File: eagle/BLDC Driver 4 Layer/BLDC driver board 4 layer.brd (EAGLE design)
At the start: 38 parts, among them Q1 CSD173XXQX-NEXFET, Q11 CSD173XXQX-NEXFET, Q3 CSD173XXQX-NEXFET, Q5 CSD173XXQX-NEXFET, Q7 CSD173XXQX-NEXFET, Q9 CSD173XXQX-NEXFET

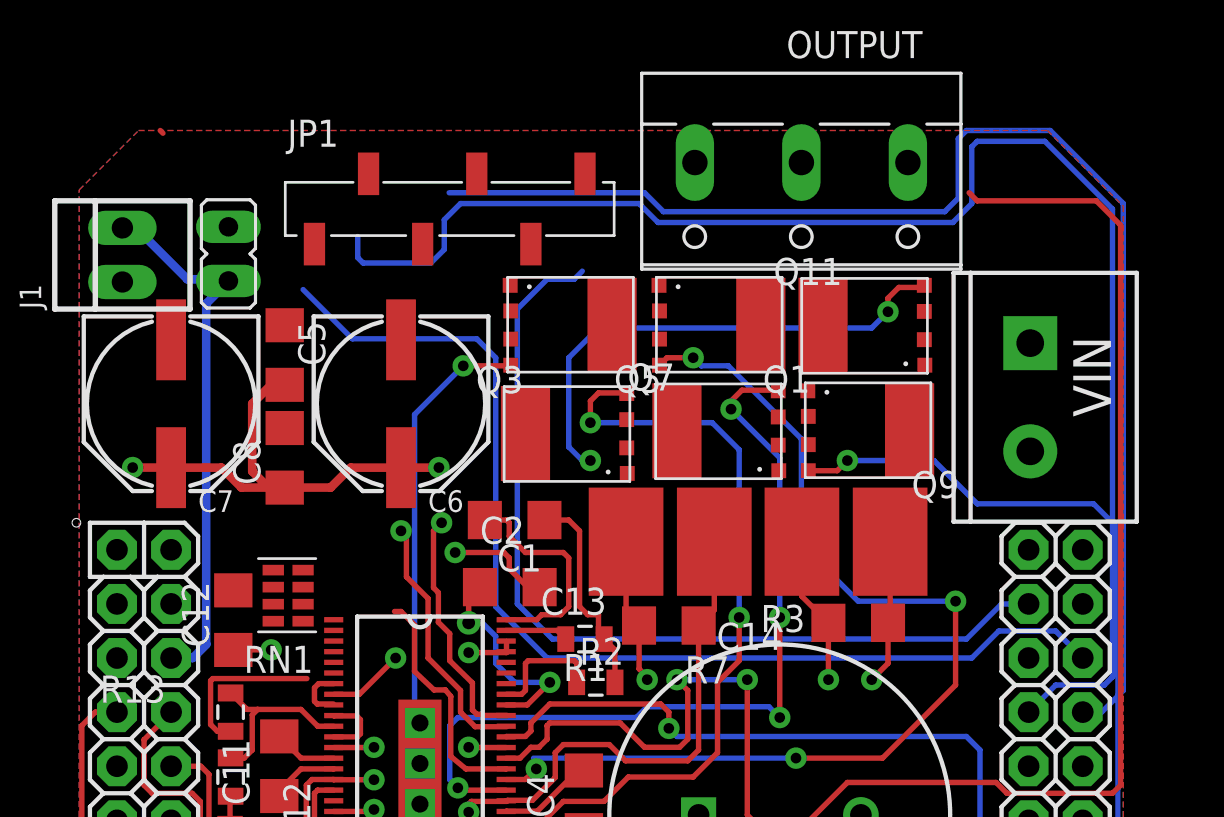
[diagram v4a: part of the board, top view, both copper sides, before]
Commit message: Changes to bldc 4-layer. Finished ethershield v3.
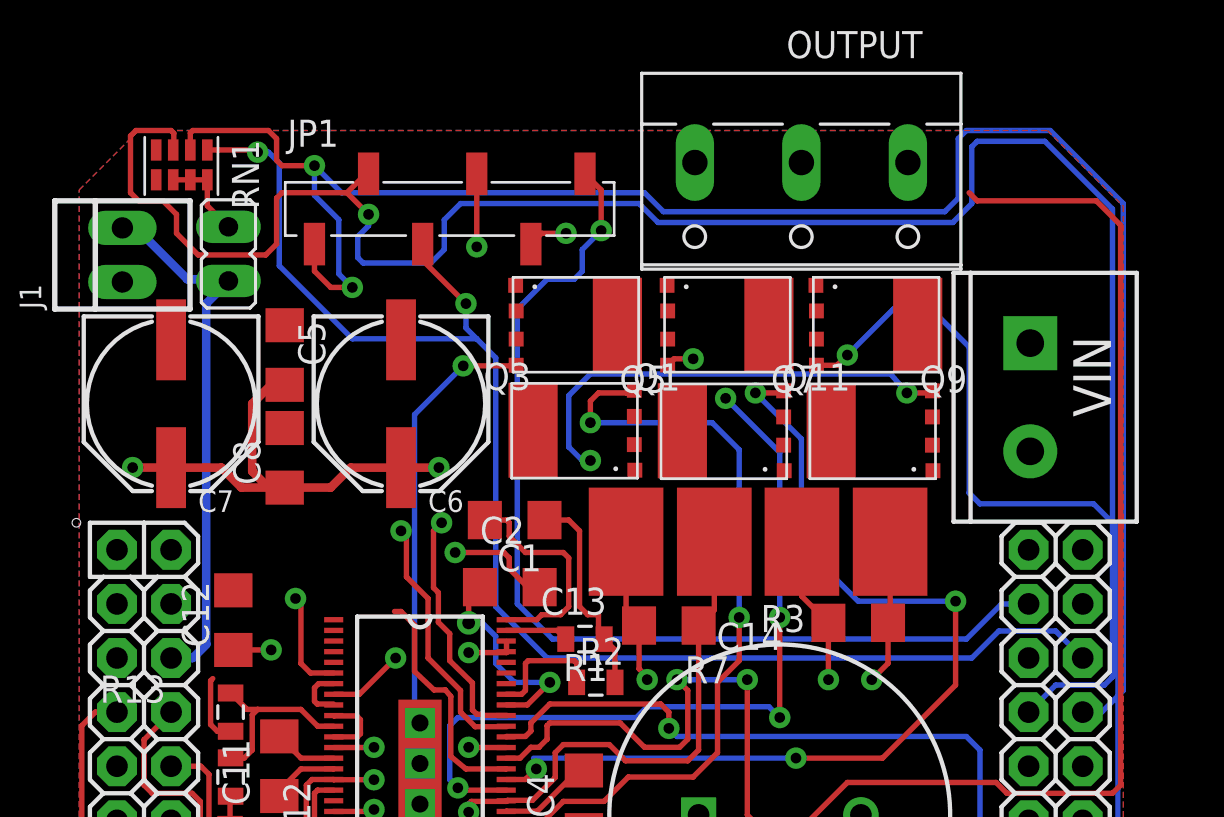
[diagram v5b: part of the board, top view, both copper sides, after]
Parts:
- moved RN1 22.6 mm to (8.69, 42.9), turned to 180 degrees
- moved Q7 6.57 mm to (35.1, 34.7), turned to 180 degrees
- moved Q1 6.17 mm to (31.0, 29.7), turned to 0 degrees
- moved Q11 4.97 mm to (38.0, 29.7)
- moved Q9 4.97 mm to (42.0, 34.7)
- moved Q3 0.39 mm to (24.0, 29.7)
- moved Q5 0.25 mm to (27.9, 34.7)
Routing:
- net ADC/HALL1: track 61.8 -> 86.5 mm, vias 0 -> 2
- net ADC/HALL2: track 70.1 -> 94.0 mm, vias 0 -> 1
- net QEI-A: track 26.4 -> 49.2 mm, vias 0 -> 1
- net N$2: track 0.00 -> 19.3 mm, vias 0 -> 1
- net ADC/HALL3: track 51.7 -> 67.2 mm, vias 0 -> 2
- net GL_A: track 71.7 -> 79.2 mm
- net QEI-INDEX: track 43.0 -> 48.3 mm, vias 0 -> 1
- net QEI-B: track 47.6 -> 52.7 mm, vias 0 -> 1
- net GND: track 24.3 -> 19.9 mm
- net N$13: track 0.00 -> 4.22 mm
- net GH_B: track 58.1 -> 54.1 mm
- net GH_A: track 43.7 -> 41.3 mm
- net GL_B: track 39.7 -> 41.8 mm, vias 4 -> 5

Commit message: Removed dependencies from ASL.lbr in /Boards.
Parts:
- DRV8301: device ASL:HTSSOP56 -> pavlo:HTSSOP56
- Q1, Q11, Q3, Q5, Q7, Q9: device ASL:CSD173XXQX -> pavlo:CSD173XXQX
- R3, R7: device ASL:SMT-REF -> pavlo:SMT-REF
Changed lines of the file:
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@@
 <?xml version="1.0" encoding="utf-8"?>
 <!DOCTYPE eagle SYSTEM "eagle.dtd">
-<eagle version="6.3">
+<eagle version="6.1">
 <drawing>
 <settings>
@@
 </class>
 </classes>
-<designrules name="default">
+<designrules>
 <description language="en">&lt;b&gt;EAGLE Design Rules&lt;/b&gt;
 &lt;p&gt;
@@
 <attribute name="VALUE" x="48.0102" y="23.7828" size="1.778" layer="27" rot="R270"/>
 </element>
-<element name="DRV8301" library="ASL" package="HTSSOP56" value="DRV8302" x="18.669" y="14.097" smashed="yes">
+<element name="DRV8301" library="pavlo" package="HTSSOP56" value="DRV8302" x="18.669" y="14.097" smashed="yes">
 <attribute name="VALUE" x="25.082" y="8.192" size="1.27" layer="27" rot="R90"/>
 </element>
@@
 <attribute name="NAME" x="11.176" y="27.178" size="1.27" layer="25" ratio="10" rot="R90"/>
 </element>
-<element name="R3" library="ASL" package="SMT-REF" value=".01" x="38.735" y="24.511" smashed="yes" rot="R180">
+<element name="R3" library="pavlo" package="SMT-REF" value=".01" x="38.735" y="24.511" smashed="yes" rot="R180">
 <attribute name="NAME" x="36.7538" y="21.5392" size="1.27" layer="25" rot="R180"/>
 </element>
-<element name="R7" library="ASL" package="SMT-REF" value=".01" x="30.48" y="24.511" smashed="yes" rot="R180">
+<element name="R7" library="pavlo" package="SMT-REF" value=".01" x="30.48" y="24.511" smashed="yes" rot="R180">
 <attribute name="NAME" x="33.1978" y="19.1262" size="1.27" layer="25" rot="R180"/>
 </element>
@@
 <attribute name="NAME" x="7.8232" y="7.0485" size="1.27" layer="25" ratio="15"/>
 </element>
-<element name="Q1" library="ASL" package="CSD173XXQX" value="CSD173XXQX-NEXFET" x="30.988" y="29.718"/>
-<element name="Q3" library="ASL" package="CSD173XXQX" value="CSD173XXQX-NEXFET" x="23.9776" y="29.7434"/>
-<element name="Q5" library="ASL" package="CSD173XXQX" value="CSD173XXQX-NEXFET" x="27.94" y="34.671" rot="R180"/>
-<element name="Q7" library="ASL" package="CSD173XXQX" value="CSD173XXQX-NEXFET" x="35.052" y="34.671" rot="R180"/>
-<element name="Q9" library="ASL" package="CSD173XXQX" value="CSD173XXQX-NEXFET" x="42.037" y="34.671" rot="R180"/>
-<element name="Q11" library="ASL" package="CSD173XXQX" value="CSD173XXQX-NEXFET" x="37.973" y="29.718"/>
+<element name="Q1" library="pavlo" package="CSD173XXQX" value="CSD173XXQX-NEXFET" x="30.988" y="29.718"/>
+<element name="Q3" library="pavlo" package="CSD173XXQX" value="CSD173XXQX-NEXFET" x="23.9776" y="29.7434"/>
+<element name="Q5" library="pavlo" package="CSD173XXQX" value="CSD173XXQX-NEXFET" x="27.94" y="34.671" rot="R180"/>
+<element name="Q7" library="pavlo" package="CSD173XXQX" value="CSD173XXQX-NEXFET" x="35.052" y="34.671" rot="R180"/>
+<element name="Q9" library="pavlo" package="CSD173XXQX" value="CSD173XXQX-NEXFET" x="42.037" y="34.671" rot="R180"/>
+<element name="Q11" library="pavlo" package="CSD173XXQX" value="CSD173XXQX-NEXFET" x="37.973" y="29.718"/>
 <element name="RN1" library="ASL" package="EXB-38V271JV" value="" x="8.6868" y="42.9006" rot="R180">
 <attribute name="OC_NEWARK" value="unknown" x="8.6868" y="42.9006" size="1.778" layer="27" rot="R180" display="off"/>

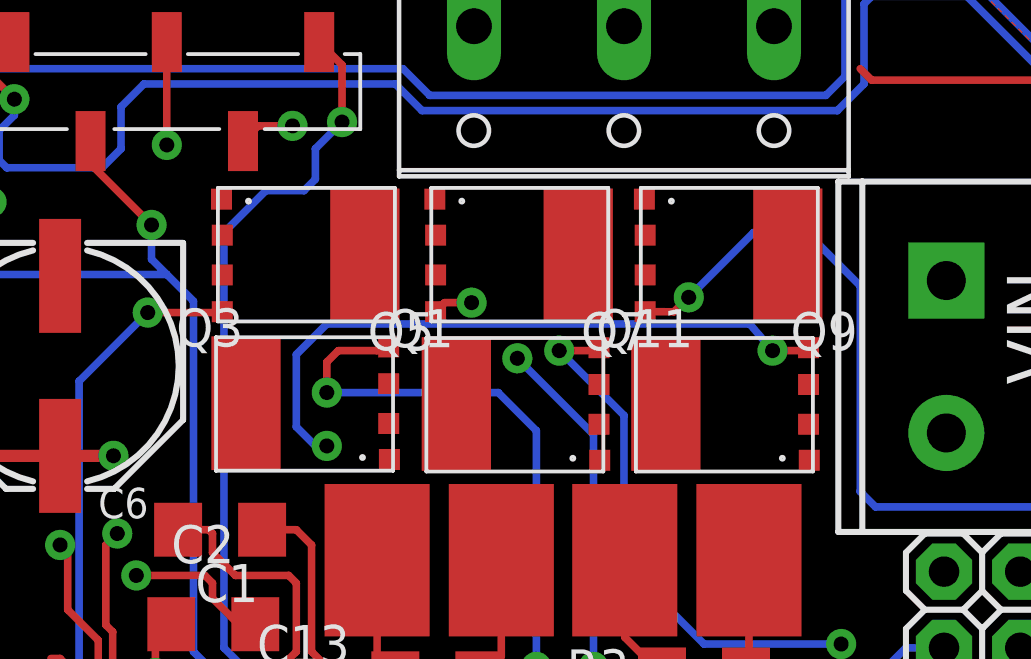
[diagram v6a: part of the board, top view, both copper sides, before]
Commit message: Updated some footprints.
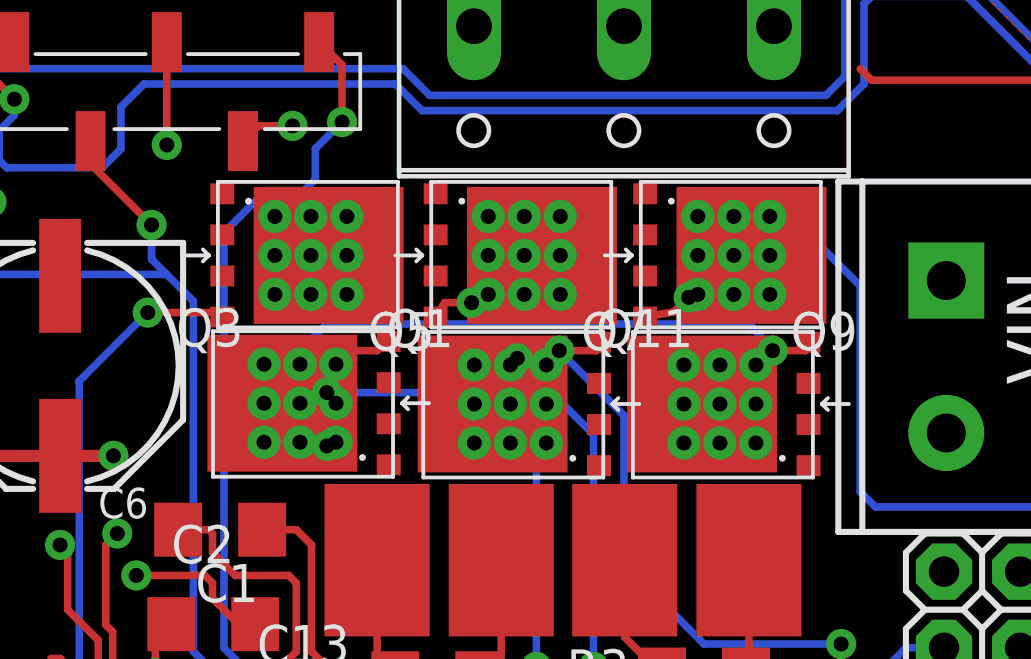
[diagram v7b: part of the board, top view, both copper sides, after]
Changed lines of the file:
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@@
 <layer number="20" name="Dimension" color="15" fill="1" visible="yes" active="yes"/>
 <layer number="21" name="tPlace" color="7" fill="1" visible="yes" active="yes"/>
-<layer number="22" name="bPlace" color="7" fill="1" visible="no" active="yes"/>
+<layer number="22" name="bPlace" color="7" fill="1" visible="yes" active="yes"/>
 <layer number="23" name="tOrigins" color="15" fill="1" visible="yes" active="yes"/>
 <layer number="24" name="bOrigins" color="15" fill="1" visible="yes" active="yes"/>
@@
 <wire x1="18.034" y1="22.86" x2="18.034" y2="24.765" width="0.254" layer="1"/>
 <wire x1="18.034" y1="24.765" x2="17.78" y2="25.019" width="0.254" layer="1"/>
-<wire x1="42.728" y1="30.368" x2="42.037" y2="34.671" width="0" layer="19" extent="1-1"/>
-<wire x1="42.728" y1="29.043" x2="42.728" y2="30.368" width="0" layer="19" extent="1-1"/>
-<wire x1="42.753" y1="27.843" x2="42.728" y2="29.043" width="0" layer="19" extent="1-1"/>
-<wire x1="41.275" y1="39.751" x2="42.037" y2="34.671" width="0" layer="19" extent="1-15"/>
+<wire x1="42.728" y1="30.403" x2="40.827" y2="34.671" width="0" layer="19" extent="1-1"/>
+<wire x1="42.728" y1="29.033" x2="42.728" y2="30.403" width="0" layer="19" extent="1-1"/>
+<wire x1="42.728" y1="27.663" x2="42.728" y2="29.033" width="0" layer="19" extent="1-1"/>
+<wire x1="41.275" y1="39.751" x2="40.827" y2="34.671" width="0" layer="19" extent="1-15"/>
 <wire x1="22.719" y1="15.847" x2="22.733" y2="15.8242" width="0" layer="19" extent="1-1"/>
 </signal>
@@
 <wire x1="43.434" y1="7.366" x2="44.45" y2="7.366" width="0.254" layer="1"/>
 <wire x1="33.782" y1="13.97" x2="38.227" y2="9.525" width="0.254" layer="15"/>
-<wire x1="35.052" y1="34.671" x2="36.576" y2="42.311" width="0" layer="19" extent="1-1"/>
-<wire x1="35.743" y1="30.368" x2="35.052" y2="34.671" width="0" layer="19" extent="1-1"/>
-<wire x1="35.743" y1="29.043" x2="35.743" y2="30.368" width="0" layer="19" extent="1-1"/>
-<wire x1="35.768" y1="27.843" x2="35.743" y2="29.043" width="0" layer="19" extent="1-1"/>
-<wire x1="33.782" y1="13.97" x2="35.768" y2="27.843" width="0" layer="19" extent="1-15"/>
+<wire x1="33.842" y1="34.671" x2="36.576" y2="42.311" width="0" layer="19" extent="1-1"/>
+<wire x1="35.743" y1="30.403" x2="33.842" y2="34.671" width="0" layer="19" extent="1-1"/>
+<wire x1="35.743" y1="29.033" x2="35.743" y2="30.403" width="0" layer="19" extent="1-1"/>
+<wire x1="35.743" y1="27.663" x2="35.743" y2="29.033" width="0" layer="19" extent="1-1"/>
+<wire x1="33.782" y1="13.97" x2="35.743" y2="27.663" width="0" layer="19" extent="1-15"/>
 <wire x1="44.46015" y1="7.35855625" x2="44.45" y2="7.366" width="0" layer="19" extent="1-1"/>
 </signal>
@@
 <wire x1="46.228" y1="12.7" x2="51.181" y2="12.7" width="0.254" layer="1"/>
 <wire x1="51.181" y1="12.7" x2="51.562" y2="13.081" width="0.254" layer="1"/>
-<wire x1="27.94" y1="34.671" x2="31.576" y2="42.311" width="0" layer="19" extent="1-1"/>
-<wire x1="28.7326" y1="30.3934" x2="27.94" y2="34.671" width="0" layer="19" extent="1-1"/>
-<wire x1="28.7326" y1="29.0684" x2="28.7326" y2="30.3934" width="0" layer="19" extent="1-1"/>
-<wire x1="28.7576" y1="27.8684" x2="28.7326" y2="29.0684" width="0" layer="19" extent="1-1"/>
+<wire x1="26.73" y1="34.671" x2="31.576" y2="42.311" width="0" layer="19" extent="1-1"/>
+<wire x1="28.7326" y1="30.4284" x2="26.73" y2="34.671" width="0" layer="19" extent="1-1"/>
+<wire x1="28.7326" y1="29.0584" x2="28.7326" y2="30.4284" width="0" layer="19" extent="1-1"/>
+<wire x1="28.7326" y1="27.6884" x2="28.7326" y2="29.0584" width="0" layer="19" extent="1-1"/>
 <wire x1="44.45" y1="40.894" x2="31.576" y2="42.311" width="0" layer="19" extent="1-1"/>
 <wire x1="51.562" y1="7.62" x2="51.181" y2="12.7" width="0" layer="19" extent="1-1"/>
@@
 <via x="41.529" y="31.496" extent="1-16" drill="0.5"/>
 <wire x1="41.529" y1="31.496" x2="42.631" y2="31.496" width="0.254" layer="1"/>
-<wire x1="42.631" y1="31.496" x2="42.728" y2="31.593" width="0.254" layer="1"/>
+<wire x1="42.631" y1="31.496" x2="42.728" y2="31.773" width="0.254" layer="1"/>
 <wire x1="22.7584" y1="16.3576" x2="22.719" y2="16.347" width="0" layer="19" extent="1-1"/>
 </signal>
@@
 <via x="38.735" y="33.274" extent="1-16" drill="0.5"/>
 <wire x1="38.735" y1="33.274" x2="38.2426" y2="32.7914" width="0.254" layer="1"/>
-<wire x1="38.2426" y1="32.7914" x2="37.282" y2="32.796" width="0.254" layer="1"/>
+<wire x1="38.2426" y1="32.7914" x2="37.282" y2="32.616" width="0.254" layer="1"/>
 <wire x1="22.733" y1="15.367" x2="22.719" y2="15.347" width="0" layer="19" extent="1-1"/>
 </signal>
@@
 <via x="34.417" y="31.496" extent="1-16" drill="0.5"/>
 <wire x1="34.417" y1="31.496" x2="35.646" y2="31.496" width="0.254" layer="1"/>
-<wire x1="35.646" y1="31.496" x2="35.743" y2="31.593" width="0.254" layer="1"/>
+<wire x1="35.646" y1="31.496" x2="35.743" y2="31.773" width="0.254" layer="1"/>
 <wire x1="22.719" y1="13.847" x2="24.003" y2="14.351" width="0" layer="19" extent="1-16"/>
 </signal>
@@
 <via x="31.496" y="33.0962" extent="1-16" drill="0.5"/>
 <wire x1="31.496" y1="33.0962" x2="30.5972" y2="33.0962" width="0.254" layer="1"/>
-<wire x1="30.5972" y1="33.0962" x2="30.297" y2="32.796" width="0.254" layer="1"/>
+<wire x1="30.5972" y1="33.0962" x2="30.297" y2="32.616" width="0.254" layer="1"/>
 </signal>
 <signal name="GH_C">
@@
 <wire x1="26.67" y1="31.115" x2="27.051" y2="31.496" width="0.254" layer="1"/>
 <wire x1="27.051" y1="31.496" x2="28.347" y2="31.496" width="0.254" layer="1"/>
-<wire x1="28.347" y1="31.496" x2="28.7326" y2="31.6184" width="0.254" layer="1"/>
+<wire x1="28.347" y1="31.496" x2="28.7326" y2="31.7984" width="0.254" layer="1"/>
 <wire x1="22.719" y1="11.347" x2="24.428" y2="11.347" width="0.254" layer="1"/>
 <wire x1="24.428" y1="11.347" x2="25.4" y2="12.319" width="0.254" layer="1"/>
@@
 <via x="20.701" y="32.766" extent="1-16" drill="0.5"/>
 <wire x1="20.701" y1="32.766" x2="22.901" y2="32.766" width="0.254" layer="1"/>
-<wire x1="22.901" y1="32.766" x2="23.185" y2="32.796" width="0.254" layer="1"/>
+<wire x1="22.901" y1="32.766" x2="23.185" y2="32.616" width="0.254" layer="1"/>
 <wire x1="22.719" y1="10.347" x2="21.911" y2="10.347" width="0.254" layer="1"/>
 <wire x1="21.911" y1="10.347" x2="21.336" y2="10.922" width="0.254" layer="1"/>
@@
 <wire x1="21.082" y1="12.319" x2="20.955" y2="12.192" width="0.254" layer="1"/>
 <wire x1="20.955" y1="12.192" x2="20.955" y2="11.811" width="0.254" layer="1"/>
-<wire x1="30.297" y1="35.346" x2="30.272" y2="36.546" width="0" layer="19" extent="1-1"/>
-<wire x1="30.297" y1="34.021" x2="30.297" y2="35.346" width="0" layer="19" extent="1-1"/>
-<wire x1="32.4866" y1="24.511" x2="30.297" y2="34.021" width="0" layer="19" extent="1-1"/>
+<wire x1="30.297" y1="35.356" x2="30.297" y2="36.726" width="0" layer="19" extent="1-1"/>
+<wire x1="30.297" y1="33.986" x2="30.297" y2="35.356" width="0" layer="19" extent="1-1"/>
+<wire x1="32.4866" y1="24.511" x2="30.297" y2="33.986" width="0" layer="19" extent="1-1"/>
 </signal>
 <signal name="SN2">
@@
 <wire x1="39.878" y1="18.0086" x2="39.878" y2="18.034" width="0.254" layer="15"/>
 <wire x1="20.955" y1="14.859" x2="35.052" y2="14.859" width="0.254" layer="15"/>
-<wire x1="37.282" y1="35.346" x2="37.257" y2="36.546" width="0" layer="19" extent="1-1"/>
-<wire x1="37.282" y1="34.021" x2="37.282" y2="35.346" width="0" layer="19" extent="1-1"/>
-<wire x1="40.7416" y1="24.511" x2="37.282" y2="34.021" width="0" layer="19" extent="1-1"/>
+<wire x1="37.282" y1="35.356" x2="37.282" y2="36.726" width="0" layer="19" extent="1-1"/>
+<wire x1="37.282" y1="33.986" x2="37.282" y2="35.356" width="0" layer="19" extent="1-1"/>
+<wire x1="40.7416" y1="24.511" x2="37.282" y2="33.986" width="0" layer="19" extent="1-1"/>
 </signal>
 <signal name="VNEG">
@@
 <wire x1="29.337" y1="18.161" x2="28.956" y2="18.542" width="0.254" layer="1"/>
 <wire x1="28.956" y1="18.542" x2="28.956" y2="20.574" width="0.254" layer="1"/>
-<wire x1="23.185" y1="35.346" x2="23.16" y2="36.546" width="0" layer="19" extent="1-1"/>
-<wire x1="23.185" y1="34.021" x2="23.185" y2="35.346" width="0" layer="19" extent="1-1"/>
-<wire x1="28.3464" y1="24.511" x2="23.185" y2="34.021" width="0" layer="19" extent="1-1"/>
+<wire x1="23.185" y1="35.356" x2="23.185" y2="36.726" width="0" layer="19" extent="1-1"/>
+<wire x1="23.185" y1="33.986" x2="23.185" y2="35.356" width="0" layer="19" extent="1-1"/>
+<wire x1="28.3464" y1="24.511" x2="23.185" y2="33.986" width="0" layer="19" extent="1-1"/>
 <wire x1="28.956" y1="20.574" x2="28.953" y2="20.574" width="0" layer="19" extent="1-1"/>
 <wire x1="22.733" y1="9.8552" x2="22.7584" y2="9.8552" width="0" layer="19" extent="1-1"/>
@@
 <wire x1="22.6822" y1="19.3548" x2="22.733" y2="19.304" width="0.254" layer="1"/>
 <wire x1="20.955" y1="19.304" x2="22.733" y2="19.304" width="0.254" layer="1"/>
-<wire x1="30.988" y1="29.718" x2="37.973" y2="29.718" width="0" layer="19" extent="1-1"/>
-<wire x1="23.9776" y1="29.7434" x2="30.988" y2="29.718" width="0" layer="19" extent="1-1"/>
-<wire x1="19.558" y1="27.9908" x2="23.9776" y2="29.7434" width="0" layer="19" extent="1-1"/>
+<wire x1="32.198" y1="29.718" x2="39.183" y2="29.718" width="0" layer="19" extent="1-1"/>
+<wire x1="25.1876" y1="29.7434" x2="32.198" y2="29.718" width="0" layer="19" extent="1-1"/>
+<wire x1="19.558" y1="27.9908" x2="25.1876" y2="29.7434" width="0" layer="19" extent="1-1"/>
 <wire x1="22.7076" y1="19.3548" x2="22.6822" y2="19.3548" width="0" layer="19" extent="1-1"/>
 <wire x1="22.719" y1="19.347" x2="22.7076" y2="19.3548" width="0" layer="19" extent="1-1"/>
